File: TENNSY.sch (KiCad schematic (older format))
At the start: 1 part, among them U1 Teensy4.0

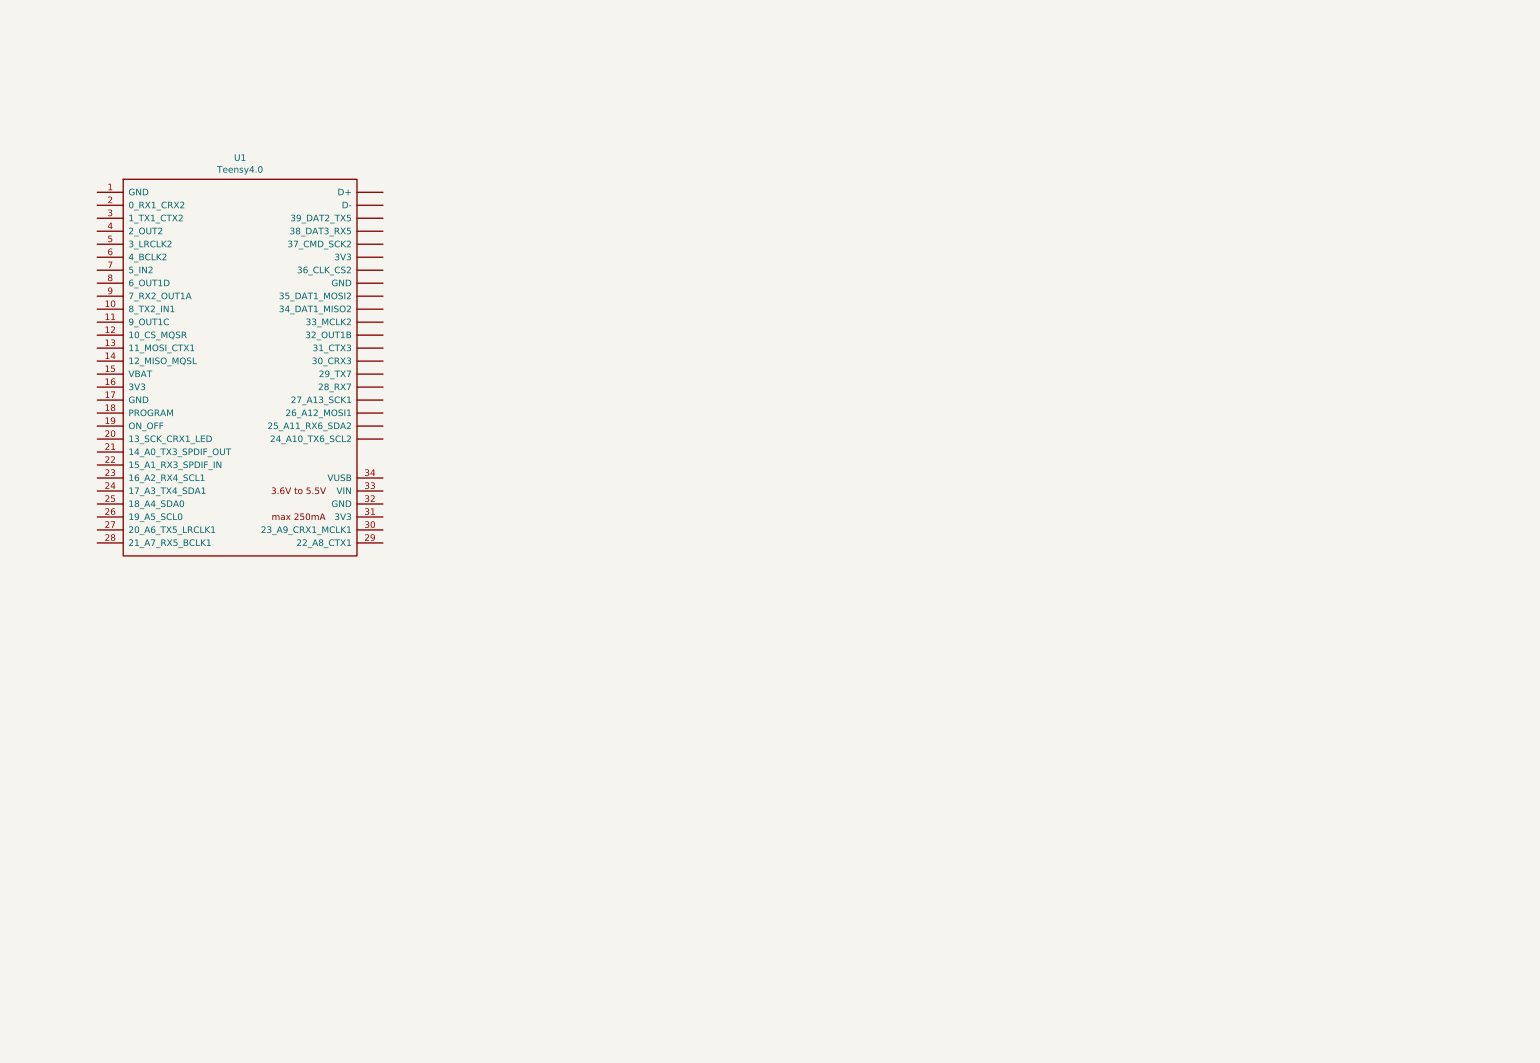
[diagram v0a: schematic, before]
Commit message: modificaciones
se arego imagenes 3d y modificacion en el sch y pcb
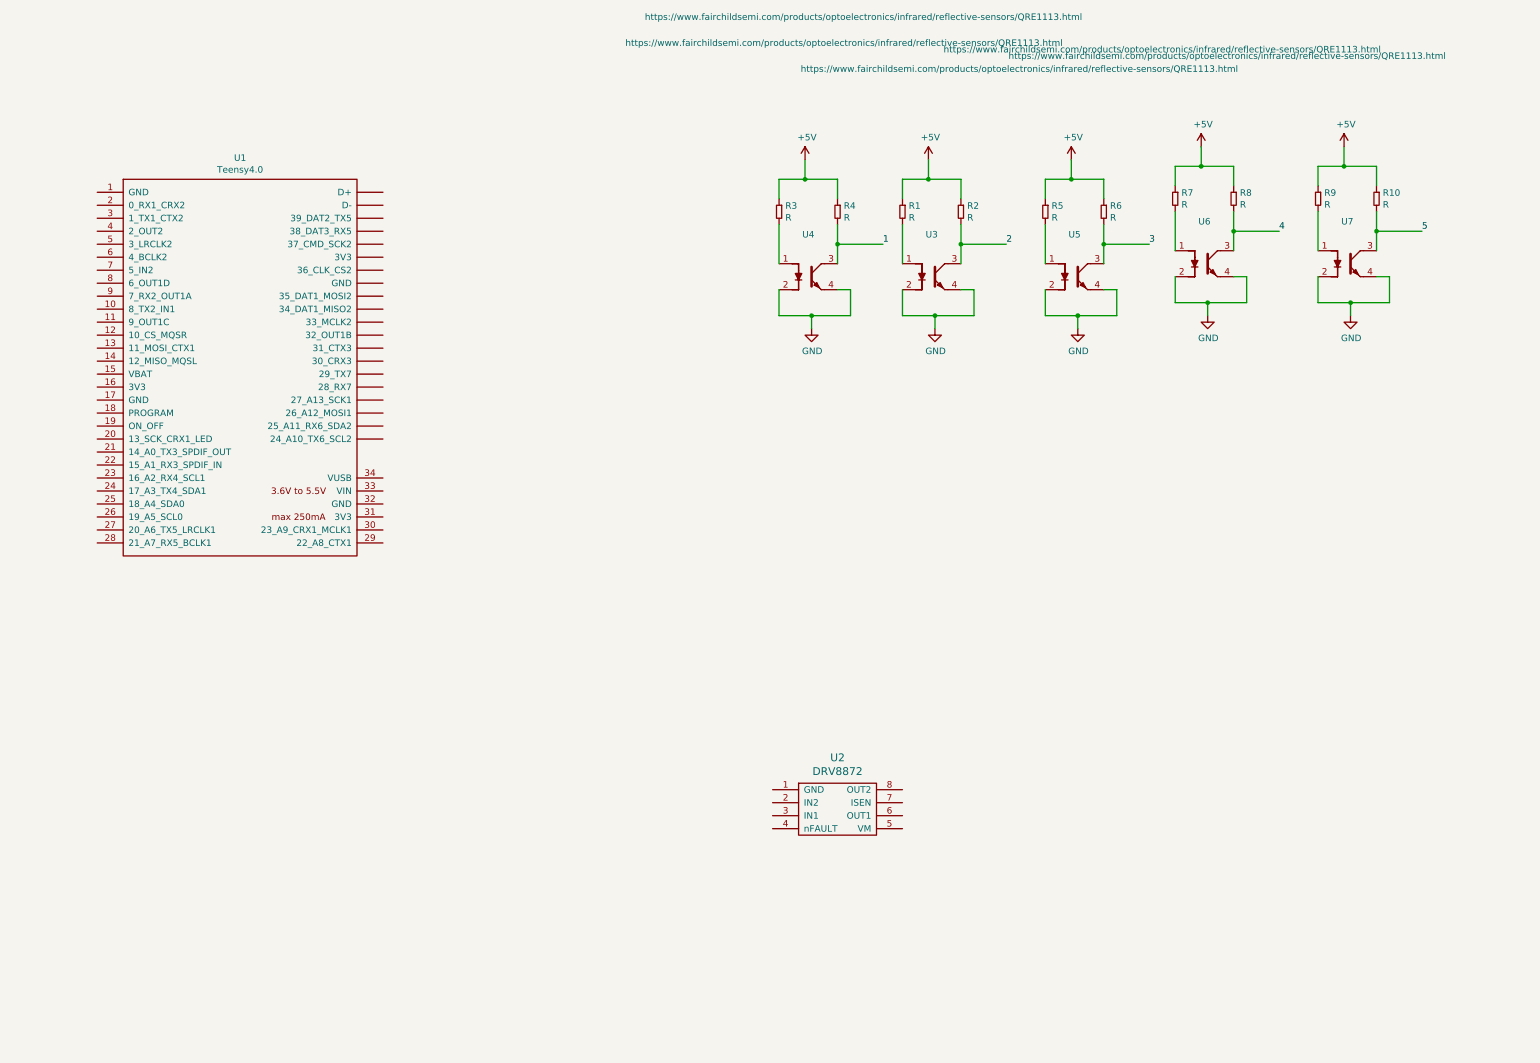
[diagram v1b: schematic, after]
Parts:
- added R1, R10, R2, R3, R4, R5, R6, R7, R8, R9: R, EESTN5:R_1206, symbol EESTN5:R
- added U2: DRV8872, EESTN5:SSOP-8, symbol EESTN5:DRV8872
- added U3, U4, U5, U6, U7: QRE1113, EESTN5:QRE1113GR, symbol EESTN5:QRE1113
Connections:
- new net: R1.2, U3.1
- new net: R5.2, U5.1
- new net: R7.2, U6.1
- new net: R9.2, U7.1
- new net: R3.2, U4.1
- new net +5V: R1.1, R10.1, R2.1, R3.1, R4.1, R5.1, R6.1, R7.1, R8.1, R9.1
- new net 1: R4.2, U4.3
- new net 2: R2.2, U3.3
- new net 3: R6.2, U5.3
- new net 4: R8.2, U6.3
- new net 5: R10.2, U7.3
- new net GND: U3.2, U3.4, U4.2, U4.4, U5.2, U5.4, U6.2, U6.4, U7.2, U7.4

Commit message: modificaciones
se modifico el pcb
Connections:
- net labels added: A0, A1, A2, A3, A6
- net labels removed: 1, 2, 3, 4, 5
- wire segments 75 -> 89
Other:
- moved on the sheet: U1, U2
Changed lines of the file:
@@
 L EESTN5:Teensy4.0 U1
 U 1 1 5FC852D2
-P 2000 2400
-F 0 "U1" H 2000 4015 50  0000 C CNN
-F 1 "Teensy4.0" H 2000 3924 50  0000 C CNN
-F 2 "EESTN5:Teensy40" H 1600 2600 50  0001 C CNN
-F 3 "" H 1600 2600 50  0001 C CNN
-	1    2000 2400
+P 2150 2400
+F 0 "U1" H 2150 4015 50  0000 C CNN
+F 1 "Teensy4.0" H 2150 3924 50  0000 C CNN
+F 2 "EESTN5:Teensy40" H 1750 2600 50  0001 C CNN
+F 3 "" H 1750 2600 50  0001 C CNN
+	1    2150 2400
 	1    0    0    -1
 $EndComp
@@
 L EESTN5:DRV8872 U2
 U 1 1 5FE72055
-P 6600 5800
-F 0 "U2" H 6600 6197 60  0000 C CNN
-F 1 "DRV8872" H 6600 6091 60  0000 C CNN
-F 2 "EESTN5:SSOP-8" H 6600 5550 60  0001 C CNN
-F 3 "" H 6600 5550 60  0001 C CNN
-	1    6600 5800
+P 5600 5950
+F 0 "U2" H 5600 6347 60  0000 C CNN
+F 1 "DRV8872" H 5600 6241 60  0000 C CNN
+F 2 "EESTN5:SSOP-8" H 5600 5700 60  0001 C CNN
+F 3 "" H 5600 5700 60  0001 C CNN
+	1    5600 5950
 	1    0    0    -1
 $EndComp
@@
 Wire Wire Line
 	7550 1450 7550 1300
-Text Label 7900 1450 0    50   ~ 0
-2
 $Comp
 L EESTN5:QRE1113 U5
@@
 Wire Wire Line
 	8650 1450 8650 1300
-Text Label 9000 1450 0    50   ~ 0
-3
 $Comp
 L EESTN5:QRE1113 U6
@@
 Wire Wire Line
 	9650 1350 9650 1200
-Text Label 10000 1350 0    50   ~ 0
-4
 $Comp
 L EESTN5:QRE1113 U7
@@
 Wire Wire Line
 	10750 1350 10750 1200
-Text Label 11100 1350 0    50   ~ 0
-5
 $Comp
 L EESTN5:QRE1113 U4
@@
 Wire Wire Line
 	6600 1450 6600 1300
+Wire Wire Line
+	1050 1050 950  1050
+Wire Wire Line
+	950  1050 950  2650
+Wire Wire Line
+	1050 2650 950  2650
+Connection ~ 950  2650
+Wire Wire Line
+	950  2650 950  4200
+Wire Wire Line
+	3250 3450 3350 3450
+Wire Wire Line
+	3350 3450 3350 4200
+$Comp
+L power:GND #PWR0111
+U 1 1 5FE4CD48
+P 3350 4200
+F 0 "#PWR0111" H 3350 3950 50  0001 C CNN
+F 1 "GND" H 3355 4027 50  0000 C CNN
+F 2 "" H 3350 4200 50  0001 C CNN
+F 3 "" H 3350 4200 50  0001 C CNN
+	1    3350 4200
+	1    0    0    -1
+$EndComp
+$Comp
+L power:GND #PWR0112
+U 1 1 5FE4D088
+P 950 4200
+F 0 "#PWR0112" H 950 3950 50  0001 C CNN
+F 1 "GND" H 955 4027 50  0000 C CNN
+F 2 "" H 950 4200 50  0001 C CNN
+F 3 "" H 950 4200 50  0001 C CNN
+	1    950  4200
+	1    0    0    -1
+$EndComp
+Wire Wire Line
+	1050 3750 850  3750
+Wire Wire Line
+	850  3650 1050 3650
+Wire Wire Line
+	1050 3550 850  3550
+Wire Wire Line
+	850  3450 1050 3450
+Wire Wire Line
+	1050 3350 850  3350
+Wire Wire Line
+	850  3250 1050 3250
+Wire Wire Line
+	1050 3150 850  3150
+Wire Wire Line
+	850  3050 1050 3050
+Text Label 850  3050 2    50   ~ 0
+A0
+Text Label 850  3150 2    50   ~ 0
+A1
+Text Label 850  3250 2    50   ~ 0
+A2
+Text Label 850  3350 2    50   ~ 0
+A3
+Text Label 850  3650 2    50   ~ 0
+A6
+Text Label 11100 1350 0    50   ~ 0
+A0
 Text Label 6950 1450 0    50   ~ 0
-1
+A6
+Text Label 7900 1450 0    50   ~ 0
+A3
+Text Label 9000 1450 0    50   ~ 0
+A2
+Text Label 10000 1350 0    50   ~ 0
+A1
 $EndSCHEMATC

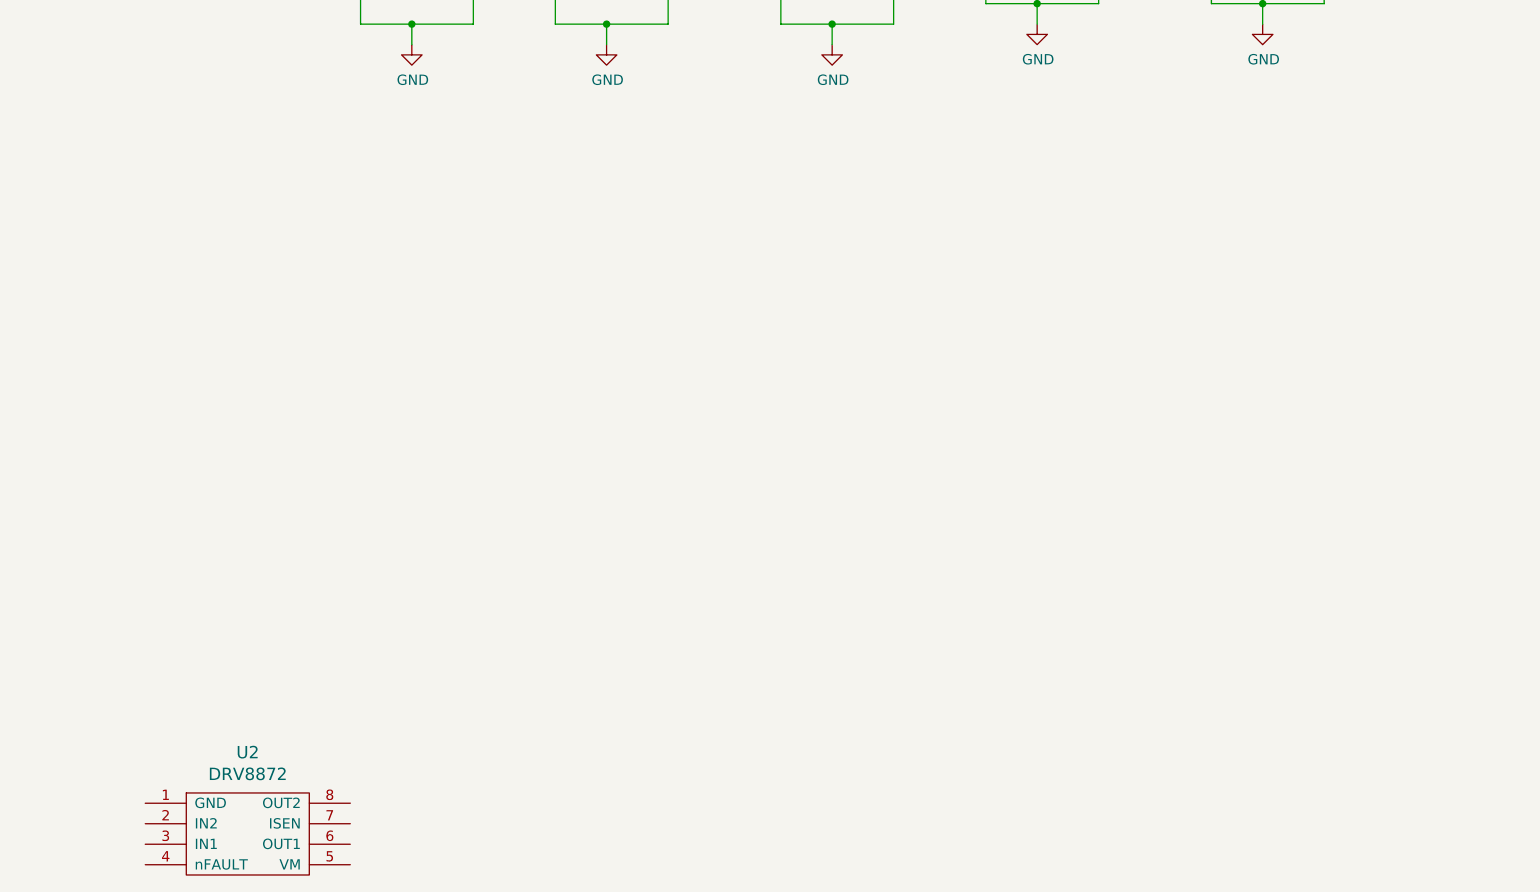
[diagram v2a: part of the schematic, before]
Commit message: modificaciones
se modifico sch,pcb y se agrego modelos 3d
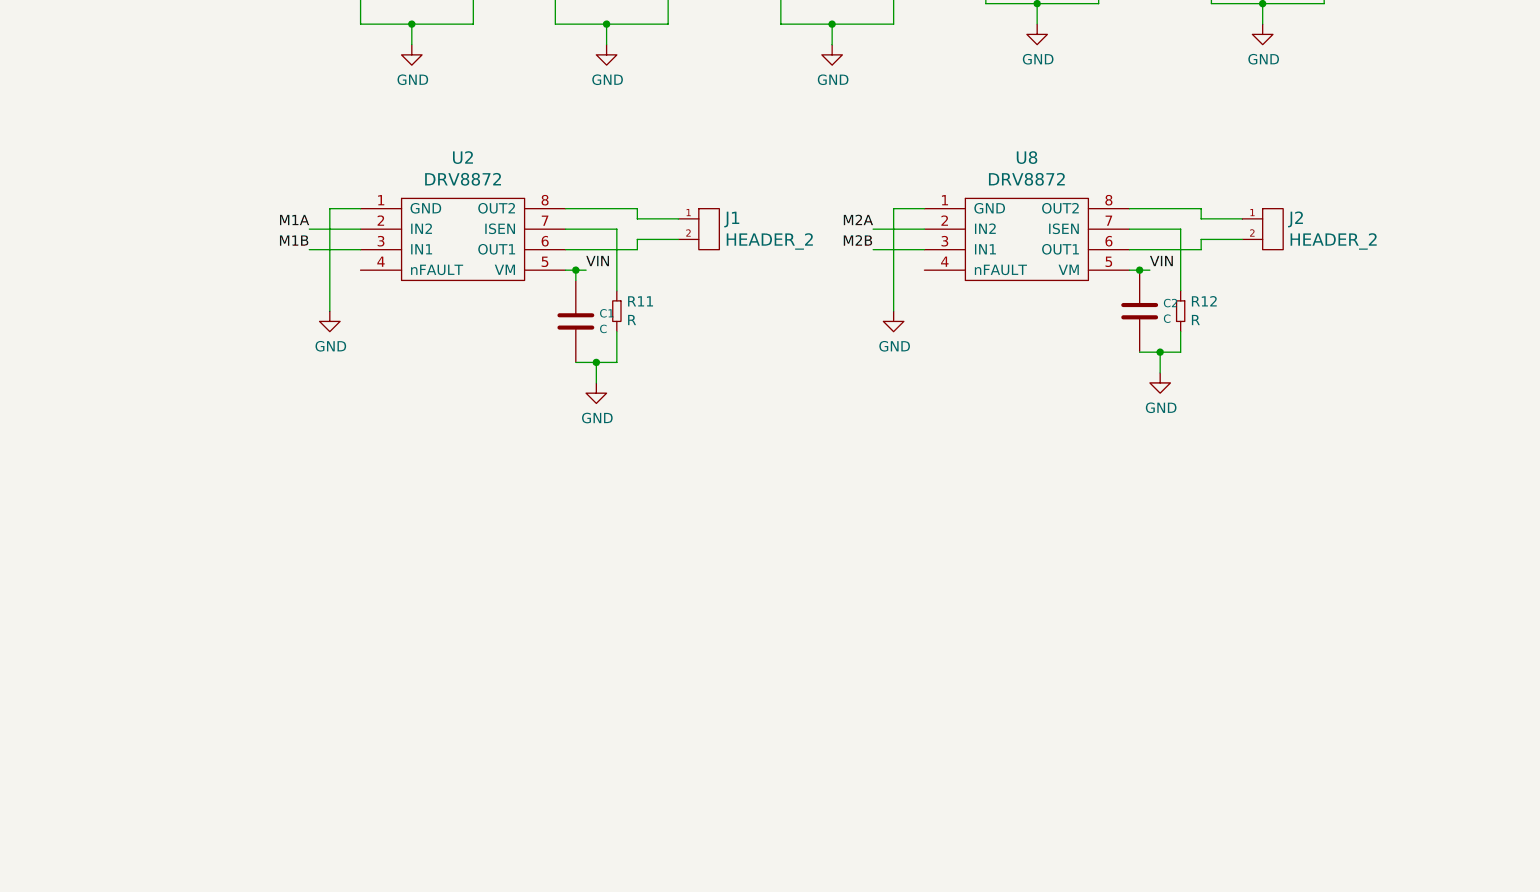
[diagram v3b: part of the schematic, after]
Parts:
- added C1, C2: C, EESTN5:CAP_ELEC_SMD_4X5.5, symbol EESTN5:C
- added J1, J2: HEADER_2, EESTN5:Pin_strip_2, symbol EESTN5:HEADER_2
- added R11, R12: R, EESTN5:R_1206, symbol EESTN5:R
- added U8: DRV8872, EESTN5:SSOP-8, symbol EESTN5:DRV8872
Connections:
- net labels added: M1A, M1B, M2A, M2B, VIN
- wire segments 89 -> 126
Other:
- moved on the sheet: U2
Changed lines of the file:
@@
 L EESTN5:DRV8872 U2
 U 1 1 5FE72055
-P 5600 5950
-F 0 "U2" H 5600 6347 60  0000 C CNN
-F 1 "DRV8872" H 5600 6241 60  0000 C CNN
-F 2 "EESTN5:SSOP-8" H 5600 5700 60  0001 C CNN
-F 3 "" H 5600 5700 60  0001 C CNN
-	1    5600 5950
+P 6650 3050
+F 0 "U2" H 6650 3447 60  0000 C CNN
+F 1 "DRV8872" H 6650 3341 60  0000 C CNN
+F 2 "EESTN5:SSOP-8" H 6650 2800 60  0001 C CNN
+F 3 "" H 6650 2800 60  0001 C CNN
+	1    6650 3050
 	1    0    0    -1
 $EndComp
@@
 Text Label 10000 1350 0    50   ~ 0
 A1
+Wire Wire Line
+	6150 3000 5900 3000
+Wire Wire Line
+	5900 3100 6150 3100
+Wire Wire Line
+	6150 2900 6000 2900
+Wire Wire Line
+	6000 2900 6000 3400
+Text Label 5900 3000 2    50   ~ 0
+M1A
+Text Label 5900 3100 2    50   ~ 0
+M1B
+$Comp
+L power:GND #PWR0113
+U 1 1 60E7B77A
+P 6000 3400
+F 0 "#PWR0113" H 6000 3150 50  0001 C CNN
+F 1 "GND" H 6005 3227 50  0000 C CNN
+F 2 "" H 6000 3400 50  0001 C CNN
+F 3 "" H 6000 3400 50  0001 C CNN
+	1    6000 3400
+	1    0    0    -1
+$EndComp
+$Comp
+L EESTN5:HEADER_2 J1
+U 1 1 60E7C223
+P 7800 3000
+F 0 "J1" H 7928 3053 60  0000 L CNN
+F 1 "HEADER_2" H 7928 2947 60  0000 L CNN
+F 2 "EESTN5:Pin_strip_2" H 7800 3250 60  0001 C CNN
+F 3 "" H 7800 3250 60  0000 C CNN
+	1    7800 3000
+	1    0    0    -1
+$EndComp
+Wire Wire Line
+	7700 2950 7500 2950
+Wire Wire Line
+	7500 2950 7500 2900
+Wire Wire Line
+	7500 2900 7150 2900
+Wire Wire Line
+	7700 3050 7500 3050
+Wire Wire Line
+	7500 3050 7500 3100
+Wire Wire Line
+	7500 3100 7150 3100
+Wire Wire Line
+	7150 3000 7400 3000
+Wire Wire Line
+	7400 3000 7400 3300
+$Comp
+L EESTN5:R R11
+U 1 1 60E85B1F
+P 7400 3400
+F 0 "R11" H 7448 3446 50  0000 L CNN
+F 1 "R" H 7448 3355 50  0000 L CNN
+F 2 "EESTN5:R_1206" H 7400 3400 60  0001 C CNN
+F 3 "" H 7400 3400 60  0000 C CNN
+	1    7400 3400
+	1    0    0    -1
+$EndComp
+Wire Wire Line
+	7400 3500 7400 3650
+$Comp
+L power:GND #PWR0114
+U 1 1 60E8935F
+P 7300 3750
+F 0 "#PWR0114" H 7300 3500 50  0001 C CNN
+F 1 "GND" H 7305 3577 50  0000 C CNN
+F 2 "" H 7300 3750 50  0001 C CNN
+F 3 "" H 7300 3750 50  0001 C CNN
+	1    7300 3750
+	1    0    0    -1
+$EndComp
+Wire Wire Line
+	7150 3200 7200 3200
+Text Label 7250 3200 0    50   ~ 0
+VIN
+$Comp
+L EESTN5:DRV8872 U8
+U 1 1 60E94CCB
+P 9400 3050
+F 0 "U8" H 9400 3447 60  0000 C CNN
+F 1 "DRV8872" H 9400 3341 60  0000 C CNN
+F 2 "EESTN5:SSOP-8" H 9400 2800 60  0001 C CNN
+F 3 "" H 9400 2800 60  0001 C CNN
+	1    9400 3050
+	1    0    0    -1
+$EndComp
+Wire Wire Line
+	8900 3000 8650 3000
+Wire Wire Line
+	8650 3100 8900 3100
+Wire Wire Line
+	8900 2900 8750 2900
+Wire Wire Line
+	8750 2900 8750 3400
+Text Label 8650 3000 2    50   ~ 0
+M2A
+Text Label 8650 3100 2    50   ~ 0
+M2B
+$Comp
+L power:GND #PWR0115
+U 1 1 60E94CDB
+P 8750 3400
+F 0 "#PWR0115" H 8750 3150 50  0001 C CNN
+F 1 "GND" H 8755 3227 50  0000 C CNN
+F 2 "" H 8750 3400 50  0001 C CNN
+F 3 "" H 8750 3400 50  0001 C CNN
+	1    8750 3400
+	1    0    0    -1
+$EndComp
+$Comp
+L EESTN5:HEADER_2 J2
+U 1 1 60E94CE5
+P 10550 3000
+F 0 "J2" H 10678 3053 60  0000 L CNN
+F 1 "HEADER_2" H 10678 2947 60  0000 L CNN
+F 2 "EESTN5:Pin_strip_2" H 10550 3250 60  0001 C CNN
+F 3 "" H 10550 3250 60  0000 C CNN
+	1    10550 3000
+	1    0    0    -1
+$EndComp
+Wire Wire Line
+	10450 2950 10250 2950
+Wire Wire Line
+	10250 2950 10250 2900
+Wire Wire Line
+	10250 2900 9900 2900
+Wire Wire Line
+	10450 3050 10250 3050
+Wire Wire Line
+	10250 3050 10250 3100
+Wire Wire Line
+	10250 3100 9900 3100
+Wire Wire Line
+	9900 3000 10150 3000
+Wire Wire Line
+	10150 3000 10150 3300
+$Comp
+L EESTN5:R R12
+U 1 1 60E94CF7
+P 10150 3400
+F 0 "R12" H 10198 3446 50  0000 L CNN
+F 1 "R" H 10198 3355 50  0000 L CNN
+F 2 "EESTN5:R_1206" H 10150 3400 60  0001 C CNN
+F 3 "" H 10150 3400 60  0000 C CNN
+	1    10150 3400
+	1    0    0    -1
+$EndComp
+Wire Wire Line
+	10150 3500 10150 3600
+Wire Wire Line
+	9900 3200 9950 3200
+Text Label 10000 3200 0    50   ~ 0
+VIN
+$Comp
+L EESTN5:C C1
+U 1 1 60E9E604
+P 7200 3450
+F 0 "C1" H 7315 3488 40  0000 L CNN
+F 1 "C" H 7315 3412 40  0000 L CNN
+F 2 "EESTN5:CAP_ELEC_SMD_4X5.5" H 7238 3300 30  0001 C CNN
+F 3 "" H 7200 3450 60  0000 C CNN
+	1    7200 3450
+	1    0    0    -1
+$EndComp
+Wire Wire Line
+	7200 3250 7200 3200
+Connection ~ 7200 3200
+Wire Wire Line
+	7200 3200 7250 3200
+Wire Wire Line
+	7200 3650 7300 3650
+Wire Wire Line
+	7300 3650 7300 3750
+Connection ~ 7300 3650
+Wire Wire Line
+	7300 3650 7400 3650
+$Comp
+L power:GND #PWR0116
+U 1 1 60EAB89F
+P 10050 3700
+F 0 "#PWR0116" H 10050 3450 50  0001 C CNN
+F 1 "GND" H 10055 3527 50  0000 C CNN
+F 2 "" H 10050 3700 50  0001 C CNN
+F 3 "" H 10050 3700 50  0001 C CNN
+	1    10050 3700
+	1    0    0    -1
+$EndComp
+$Comp
+L EESTN5:C C2
+U 1 1 60EAB8A9
+P 9950 3400
+F 0 "C2" H 10065 3438 40  0000 L CNN
+F 1 "C" H 10065 3362 40  0000 L CNN
+F 2 "EESTN5:CAP_ELEC_SMD_4X5.5" H 9988 3250 30  0001 C CNN
+F 3 "" H 9950 3400 60  0000 C CNN
+	1    9950 3400
+	1    0    0    -1
+$EndComp
+Wire Wire Line
+	9950 3600 10050 3600
+Wire Wire Line
+	10050 3600 10050 3700
+Connection ~ 10050 3600
+Wire Wire Line
+	10050 3600 10150 3600
+Connection ~ 9950 3200
+Wire Wire Line
+	9950 3200 10000 3200
 $EndSCHEMATC
